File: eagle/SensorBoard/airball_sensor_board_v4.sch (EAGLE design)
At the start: 66 parts, among them J2 AVR_SPI_PROG_3X2PTH, U2 MCP73831, U3 MIC5219 3.3V, Y1 8MHz

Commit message: Add newest WIP for airball_sensor_board_v4 and STL
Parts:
- removed U$2: DS2782, airball:DS2782
- removed U2: MCP73831, SparkFun-IC-Power:MCP73831
- removed U3: MIC5219 3.3V, SparkFun-IC-Power:V_REG_MIC52193.3V
- added BM: DS2782, airball:DS2782
- added C16: 10uF, SparkFun-Capacitors:10UF-POLAR-0603-6.3V-20%(TANT)
- added CC: MCP73831, SparkFun-IC-Power:MCP73831
- added D7: (no value), SparkFun-LED:LED0603
- added F2: 6V/0.5A, SparkFun-Fuses:PPTC_HALF-AMP
- added VREG: LT1963, airball:LT1963
- OAT: value TMP102 -> TMP275; device SparkFun-Sensors:TMP102 -> airball:LM75-8PIN
- R13: device SparkFun-Resistors:RESISTOR0603 -> SparkFun-Resistors:RESISTOR1206
- renumbered U$1 to MCU, U1 to MUX, XB1 to XBEE
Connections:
- net N$15 renamed ASSOC_LED
- net N$17 renamed RSSI_LED
- net N$18 renamed ON_LED
- net N$8 renamed TX_LED
- net N$9 renamed RX_LED
- removed net BAT_GND: J1.-, JP1.GND, R13.1, R15.1, U$2.VSS, U2.VSS
- removed net N$11: R15.2, U2.PROG
- removed net N$13: MCU.!RESET, R23.2
- removed net N$2: R18.1, U2.STAT
- removed net N$3: D1.A, J1.+, S1.P, U2.VBAT
- removed net N$4: R11.1, U$2.VIN
- removed net N$5: R12.1, U$2.VDD
- removed net VCC_5V0_UF: F1.1, JP1.VCC
- new net BAT+: C16.+, CC.VBAT, D2.A, F2.2, R11.2, R12.2, S1.P
- new net BAT+_UF: F2.1, J1.+
- new net BAT-: BM.VSS, J1.-, R13.1
- new net BM_VDD: BM.VDD, R12.1
- new net BM_VIN: BM.VIN, R11.1
- new net CC_PROG: CC.PROG, R15.2
- new net CHG_LED: CC.STAT, R18.1
- net BAT_VRAW: now also VREG.IN; no longer R11.2, R12.2, U3.EN, U3.IN
- net GND: now also BM.SNS, C16.-, CC.VSS, D1.A, D7.C, JP1.GND, OAT.ADD1, OAT.ADD2, R15.1, VREG.GND; no longer D2.C, U$2.SNS, U3.GND
- net N$1: now also D2.C
- net N$10: now also D3.A; no longer D2.A
- net N$14: now also D4.A; no longer D3.A
- net N$20: now also D5.A; no longer D4.A
- net N$21: now also D6.A; no longer D5.A
- net N$22: now also D7.A; no longer D6.A
- net RST: now also MCU.!RESET, R23.2
- net SCL_BM: now also BM.SCL; no longer U$2.SCL
- net SDA_BM: now also BM.SDA; no longer U$2.SDA
- net USB_5V0_UF: now also F1.1, JP1.VCC; no longer C13.2, MCU.UVCC, MCU.VBUS
- net VCC_3V3: now also VREG.OUT; no longer U3.OUT
- net VCC_5V0: now also C13.2, CC.VIN, MCU.UVCC, MCU.VBUS; no longer U2.VIN
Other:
- note added: "Battery Charging Status"
- note added: "Battery Fuse"
- note added: "TODO:"
- note added: "TODO: * Replace 3.3V regulator with bigger one"
- note added: "USB Fuse"
- note removed: "Charging Status"
- note removed: "Resettable Fuse"
- note removed: "TODO: Replace TMP102 with ???"
- moved on the sheet: D1, D3, D4, D5, D6, F1, J1, JP1, R11, R12, R13, R15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

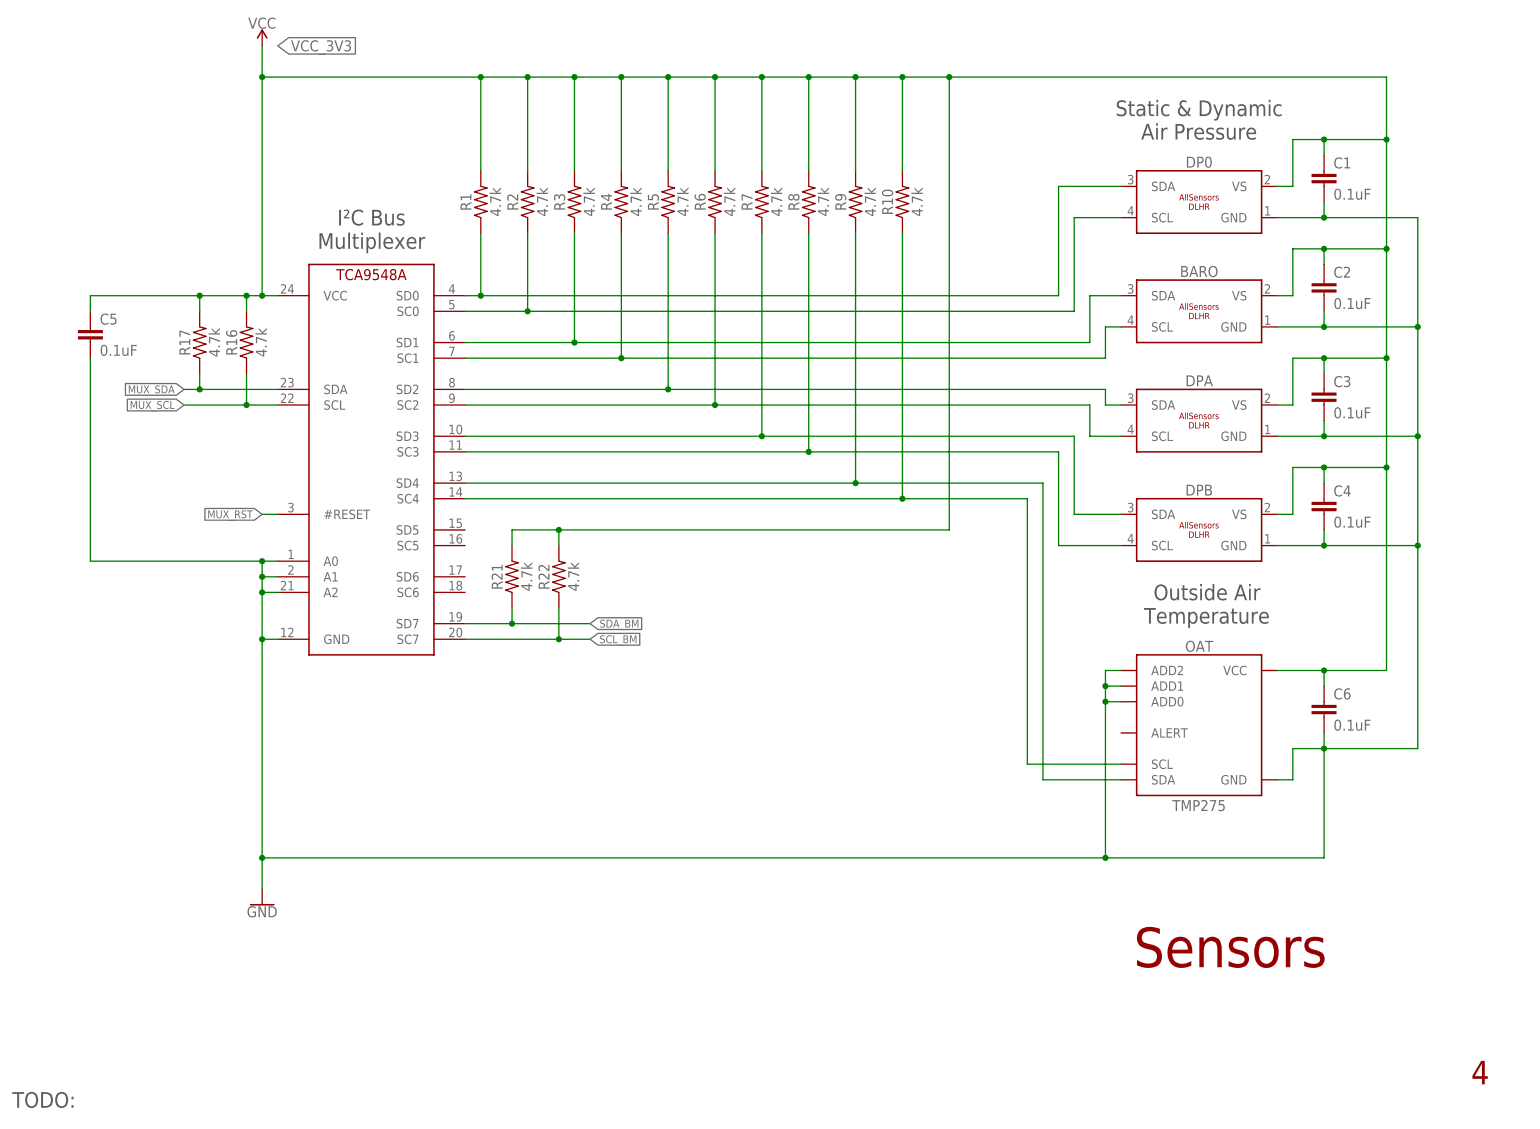
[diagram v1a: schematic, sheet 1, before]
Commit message: Updated airball_sensor_board_v4 and library; added as-ordered gerbers
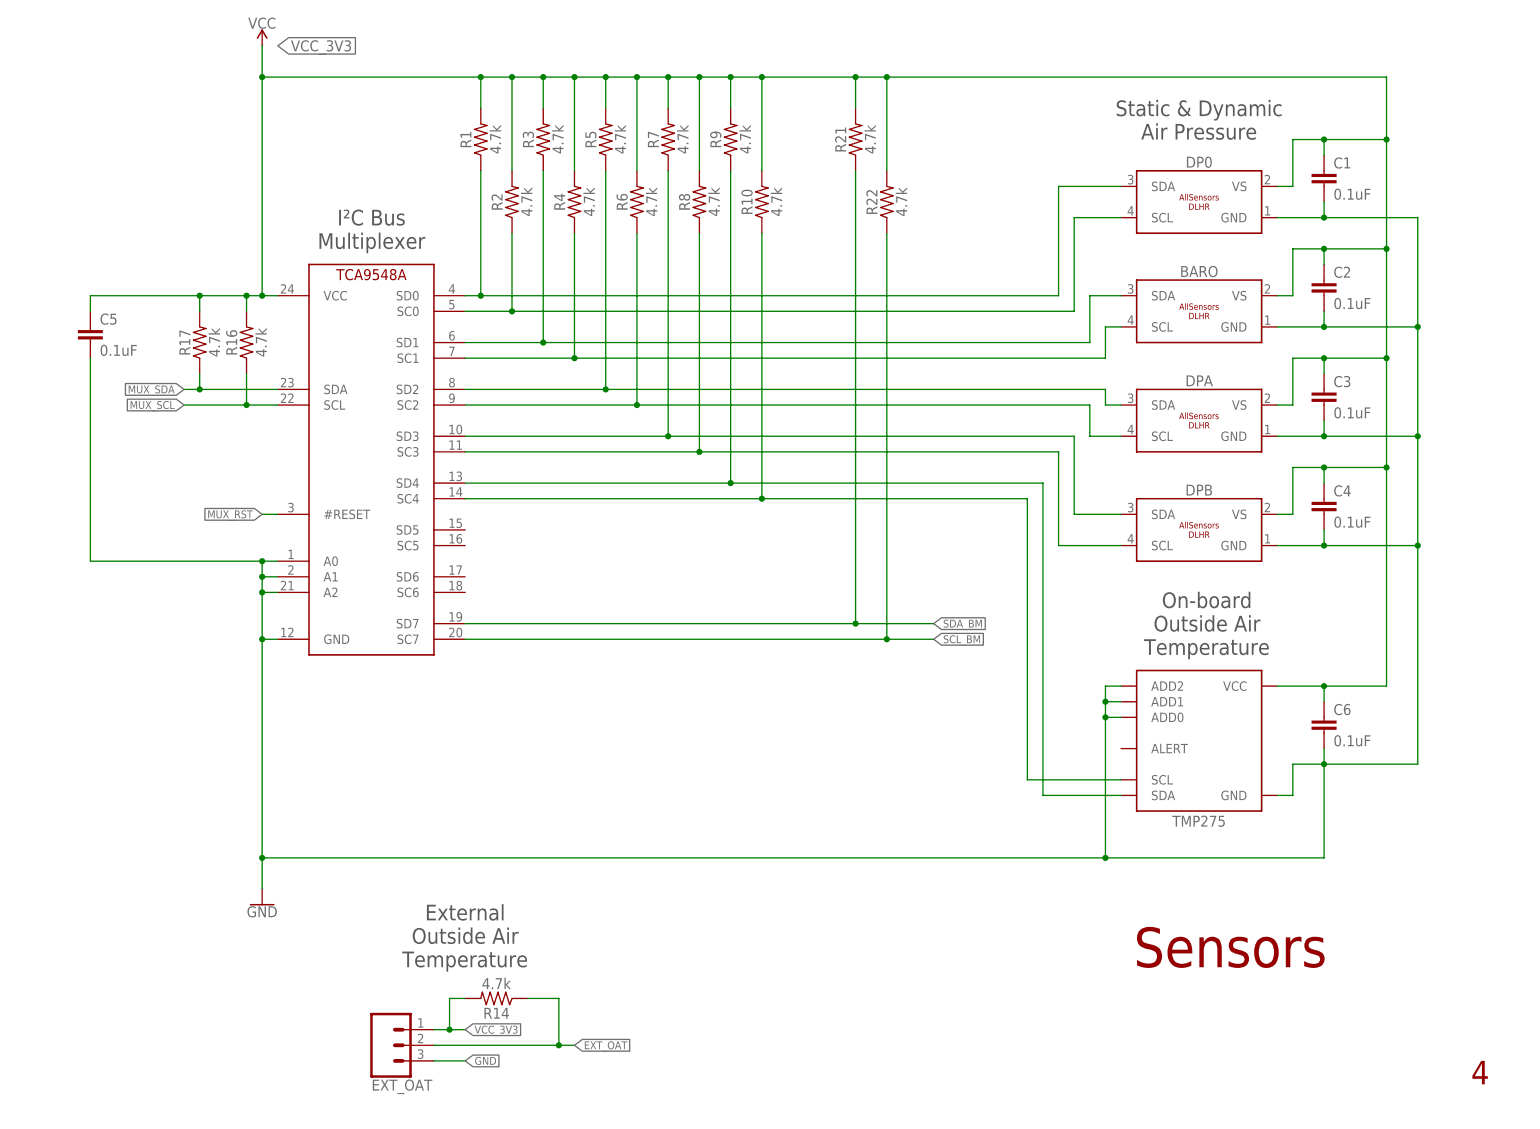
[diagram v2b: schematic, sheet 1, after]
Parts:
- added C17, C18, C19: 10uF, SparkFun-Capacitors:10UF-POLAR-EIA3216-16V-10%(TANT)
- added EXT_OAT: (no value), SparkFun-Connectors:CONN_03
- added EXT_POWER, EXT_SW: (no value), SparkFun-Connectors:CONN_02
- added R14: 4.7k, SparkFun-Resistors:4.7KOHM-0603-1/10W-1%
- C16, C7: device SparkFun-Capacitors:10UF-POLAR-0603-6.3V-20%(TANT) -> SparkFun-Capacitors:10UF-POLAR-EIA3216-16V-10%(TANT)
- renumbered J2 to ICSP
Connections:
- net RX renamed RXD
- net TX renamed TXD
- new net EXT_OAT: EXT_OAT.2, MCU.PF0(ADC0), R14.1
- net BAT+: now also EXT_SW.1
- net BAT_VRAW: now also EXT_SW.2
- net GND: now also C17.-, C18.-, C19.-, EXT_OAT.3, EXT_POWER.2
- net USB_5V0_UF: now also EXT_POWER.1
- net VCC_3V3: now also C17.+, C18.+, C19.+, EXT_OAT.1, R14.2
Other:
- note added: "5V Input"
- note added: "Battery Charge Controller"
- note added: "Battery Status"
- note added: "CHG."
- note added: "External Outside Air Temperature"
- note added: "FULL"
- note added: "MCU/Radio"
- note added: "On-board Outside Air Temperature"
- note added: "On-board and External Power Switch"
- note added: "Regulated 3.3V Output"
- note removed: "Battery Charging Status"
- note removed: "Battery Fuse"
- note removed: "Charge Controller"
- note removed: "Outside Air Temperature"
- note removed: "Power Switch"
- note removed: "Processing/Radio"
- note removed: "Regulated Output"
- note removed: "TODO:"
- note removed: "TODO: * Replace 3.3V regulator with bigger one"
- note removed: "USB Fuse"
- moved on the sheet: C6, D1, D2, R1, R10, R18, R2, R21, R22, R23, R3, R4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

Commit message: Minor cleanups to sensor v4
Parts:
- BARO, DP0, DPA, DPB: value ALLSENSORS_DLHR_I2C-E1BD -> (none)
